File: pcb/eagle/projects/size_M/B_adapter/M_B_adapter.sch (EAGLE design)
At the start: 16 parts

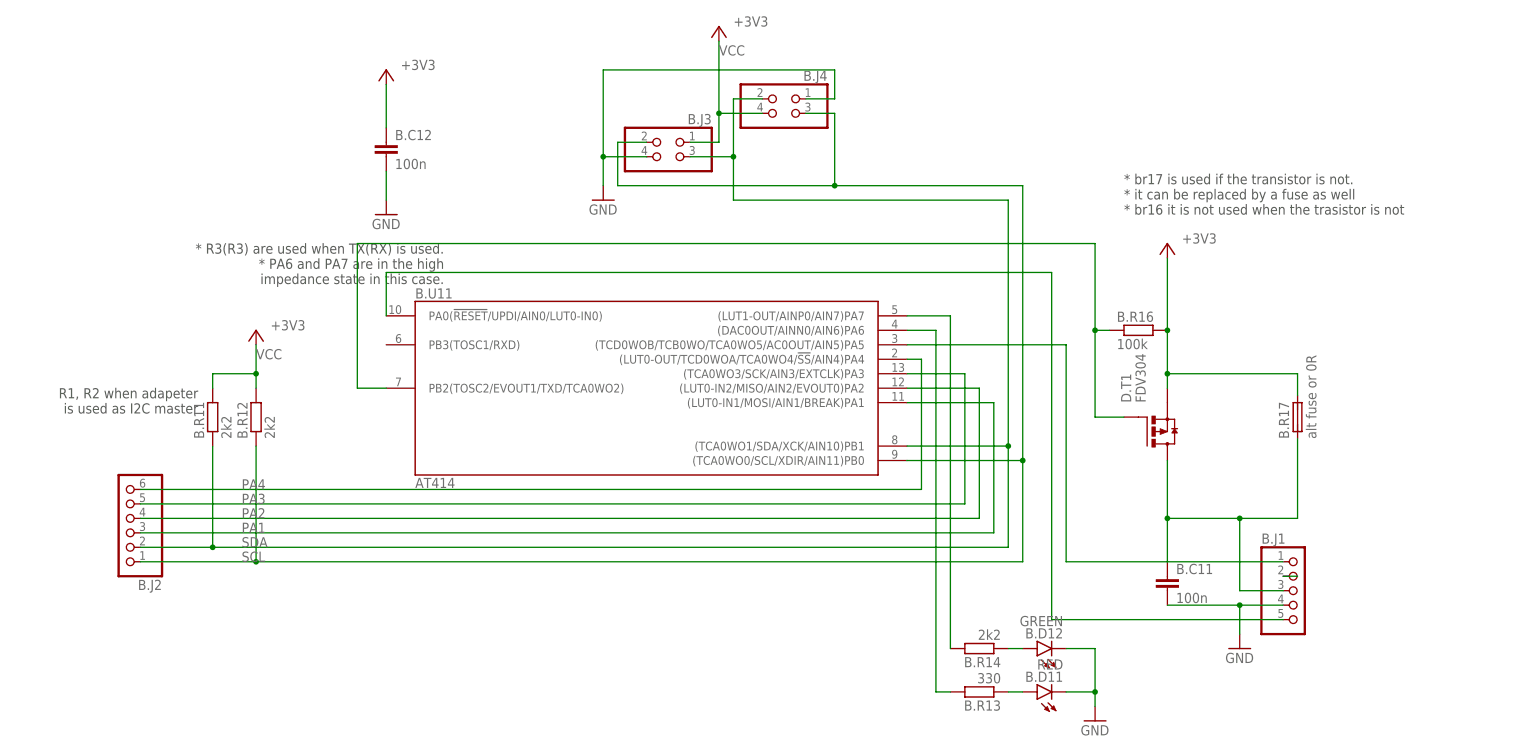
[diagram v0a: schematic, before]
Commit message: version 8 main changes * ideal diode separated 3v3 DC-DC to protect it from back current * smaller package of ina 219 * usage of tssop attiny v2 in adapter * and change of PA5 to PB2 with ^ and ~ (originally used for shield power switch - now PB3) * step motor shield * out signal for BT module
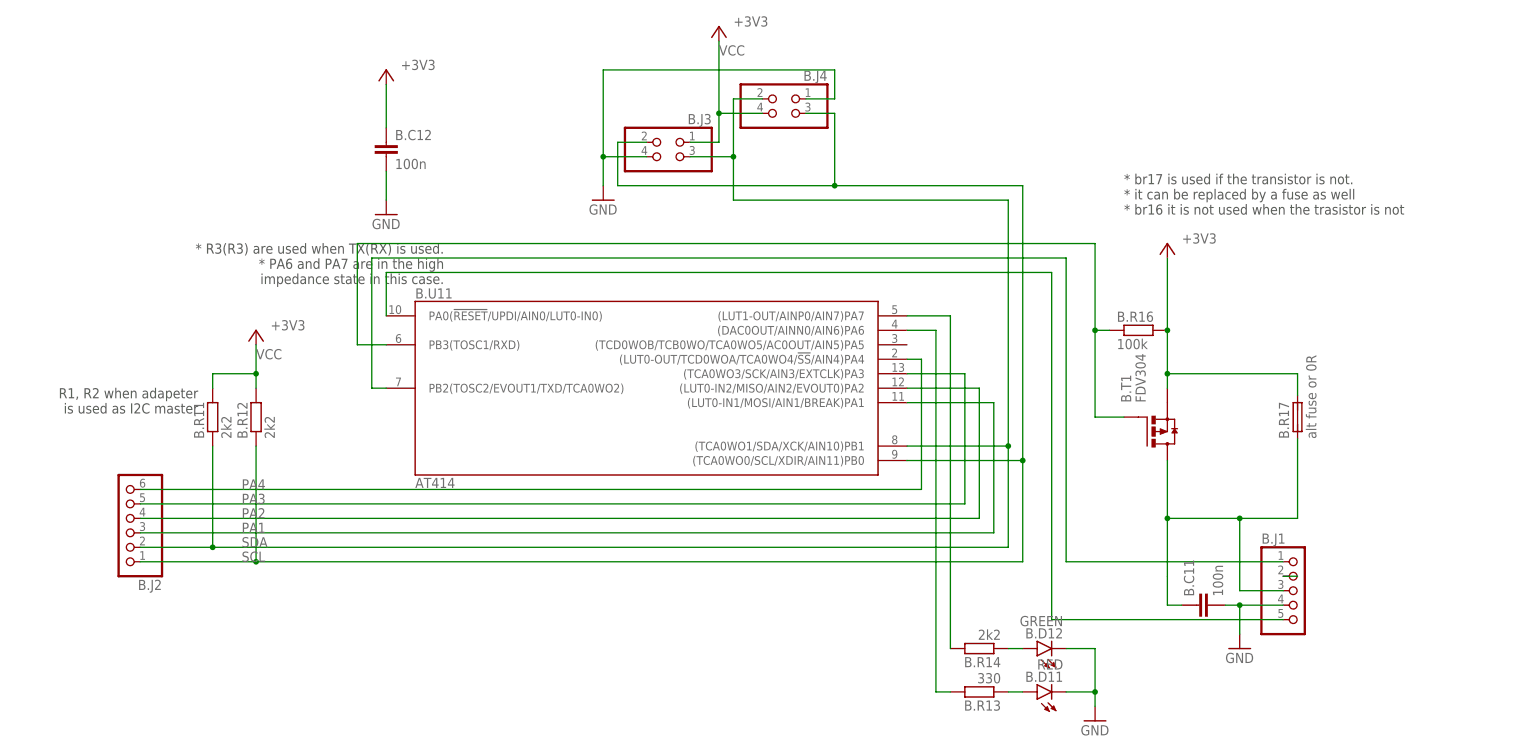
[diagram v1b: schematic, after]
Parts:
- renumbered D.T1 to B.T1
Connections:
- removed net PA5: B.J1.1, B.U11G$1.(TCD0WOB/TCB0WO/TCA0WO5/AC0OUT/AIN5)PA5
- new net PB3: B.R16.1, B.T1.G, B.U11G$1.PB3(TOSC1/RXD)
- net PB2: now also B.J1.1; no longer B.R16.1, B.T1.G
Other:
- moved on the sheet: B.C11
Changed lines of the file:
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@@
 <part name="B.R14" library="rcl" library_urn="urn:adsk.eagle:library:334" deviceset="R-EU_" device="R0603" package3d_urn="urn:adsk.eagle:package:23555/3" value="2k2"/>
 <part name="B.D12" library="led" deviceset="LED" device="CHIP-LED0603" package3d_urn="urn:adsk.eagle:package:15819/3" value="GREEN"/>
-<part name="D.T1" library="hugo" deviceset="P-MOSFET" device="" value="FDV304"/>
+<part name="B.T1" library="hugo" deviceset="P-MOSFET" device="" value="FDV304"/>
 </parts>
 <sheets>
@@
 <attribute name="VALUE" x="143.51" y="71.12" size="1.778" layer="96" rot="MR0"/>
 </instance>
-<instance part="B.C11" gate="G$1" x="203.2" y="-5.08" smashed="yes">
-<attribute name="NAME" x="204.724" y="-4.699" size="1.778" layer="95"/>
-<attribute name="VALUE" x="204.724" y="-9.779" size="1.778" layer="96"/>
+<instance part="B.C11" gate="G$1" x="208.28" y="-10.16" smashed="yes" rot="R90">
+<attribute name="NAME" x="207.899" y="-8.636" size="1.778" layer="95" rot="R90"/>
+<attribute name="VALUE" x="212.979" y="-8.636" size="1.778" layer="96" rot="R90"/>
 </instance>
 <instance part="B.J1" gate="A" x="226.06" y="-7.62" smashed="yes">
@@
 <attribute name="VALUE" x="184.912" y="-12.065" size="1.778" layer="96" rot="R180"/>
 </instance>
-<instance part="D.T1" gate="G$1" x="200.66" y="22.86" smashed="yes">
+<instance part="B.T1" gate="G$1" x="200.66" y="22.86" smashed="yes">
 <attribute name="NAME" x="196.85" y="25.4" size="1.778" layer="95" rot="R90"/>
 <attribute name="VALUE" x="199.39" y="25.4" size="1.778" layer="96" rot="R90"/>
@@
 <pinref part="B.C11" gate="G$1" pin="2"/>
 <pinref part="B.J1" gate="A" pin="4"/>
-<wire x1="203.2" y1="-10.16" x2="215.9" y2="-10.16" width="0.1524" layer="91"/>
+<wire x1="213.36" y1="-10.16" x2="215.9" y2="-10.16" width="0.1524" layer="91"/>
 <wire x1="215.9" y1="-10.16" x2="223.52" y2="-10.16" width="0.1524" layer="91"/>
 <pinref part="GND2" gate="1" pin="GND"/>
@@
 <pinref part="B.R17" gate="G$1" pin="2"/>
 <wire x1="226.06" y1="26.67" x2="226.06" y2="30.48" width="0.1524" layer="91"/>
-<pinref part="D.T1" gate="G$1" pin="S"/>
+<pinref part="B.T1" gate="G$1" pin="S"/>
 <pinref part="B.R16" gate="G$1" pin="2"/>
 <junction x="203.2" y="38.1"/>
@@
 <pinref part="B.C11" gate="G$1" pin="1"/>
 <wire x1="203.2" y1="15.24" x2="203.2" y2="5.08" width="0.1524" layer="91"/>
-<wire x1="203.2" y1="5.08" x2="203.2" y2="-2.54" width="0.1524" layer="91"/>
+<wire x1="203.2" y1="5.08" x2="203.2" y2="-5.08" width="0.1524" layer="91"/>
+<wire x1="203.2" y1="-5.08" x2="203.2" y2="-10.16" width="0.1524" layer="91"/>
+<wire x1="203.2" y1="-10.16" x2="205.74" y2="-10.16" width="0.1524" layer="91"/>
 <wire x1="203.2" y1="5.08" x2="215.9" y2="5.08" width="0.1524" layer="91"/>
 <wire x1="215.9" y1="5.08" x2="215.9" y2="-7.62" width="0.1524" layer="91"/>
@@
 <wire x1="215.9" y1="5.08" x2="226.06" y2="5.08" width="0.1524" layer="91"/>
 <wire x1="226.06" y1="5.08" x2="226.06" y2="19.05" width="0.1524" layer="91"/>
-<pinref part="D.T1" gate="G$1" pin="D"/>
+<pinref part="B.T1" gate="G$1" pin="D"/>
 </segment>
 </net>
@@
 </segment>
 </net>
-<net name="PB2" class="0">
+<net name="PB3" class="0">
 <segment>
 <wire x1="195.58" y1="22.86" x2="190.5" y2="22.86" width="0.1524" layer="91"/>
@@
 <wire x1="190.5" y1="38.1" x2="190.5" y2="53.34" width="0.1524" layer="91"/>
 <wire x1="190.5" y1="53.34" x2="60.96" y2="53.34" width="0.1524" layer="91"/>
-<wire x1="60.96" y1="53.34" x2="60.96" y2="27.94" width="0.1524" layer="91"/>
-<pinref part="B.U11" gate="G$1" pin="PB2(TOSC2/EVOUT1/TXD/TCA0WO2)"/>
-<wire x1="60.96" y1="27.94" x2="66.04" y2="27.94" width="0.1524" layer="91"/>
-<pinref part="D.T1" gate="G$1" pin="G"/>
+<wire x1="60.96" y1="53.34" x2="60.96" y2="35.56" width="0.1524" layer="91"/>
+<pinref part="B.T1" gate="G$1" pin="G"/>
 <pinref part="B.R16" gate="G$1" pin="1"/>
 <wire x1="193.04" y1="38.1" x2="190.5" y2="38.1" width="0.1524" layer="91"/>
 <junction x="190.5" y="38.1"/>
+<pinref part="B.U11" gate="G$1" pin="PB3(TOSC1/RXD)"/>
+<wire x1="66.04" y1="35.56" x2="60.96" y2="35.56" width="0.1524" layer="91"/>
 </segment>
 </net>
@@
 </segment>
 </net>
-<net name="PA5" class="0">
+<net name="PB2" class="0">
 <segment>
 <pinref part="B.J1" gate="A" pin="1"/>
-<wire x1="185.42" y1="35.56" x2="185.42" y2="-2.54" width="0.1524" layer="91"/>
+<wire x1="185.42" y1="50.8" x2="185.42" y2="-2.54" width="0.1524" layer="91"/>
 <wire x1="185.42" y1="-2.54" x2="223.52" y2="-2.54" width="0.1524" layer="91"/>
-<pinref part="B.U11" gate="G$1" pin="(TCD0WOB/TCB0WO/TCA0WO5/AC0OUT/AIN5)PA5"/>
-<wire x1="157.48" y1="35.56" x2="185.42" y2="35.56" width="0.1524" layer="91"/>
-</segment>
-</net>
+<pinref part="B.U11" gate="G$1" pin="PB2(TOSC2/EVOUT1/TXD/TCA0WO2)"/>
+<wire x1="63.5" y1="27.94" x2="66.04" y2="27.94" width="0.1524" layer="91"/>
+<wire x1="185.42" y1="50.8" x2="63.5" y2="50.8" width="0.1524" layer="91"/>
+<wire x1="63.5" y1="50.8" x2="63.5" y2="27.94" width="0.1524" layer="91"/>
+</segment>
+</net>

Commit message: PCB v9
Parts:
- removed B.J1: (no value), pinhead2:PINHD-1X5
- added B.J5: (no value), pinhead2:PINHD-1X6
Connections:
- new net PA6: B.J5.1, B.U11G$1.(DAC0OUT/AINN0/AIN6)PA6
- net GND: now also B.J5.4; no longer B.J1.4
- net N$4: now also B.J5.3; no longer B.J1.3
- net N$5: now also B.U11G$1.(TCD0WOB/TCB0WO/TCA0WO5/AC0OUT/AIN5)PA5; no longer B.U11G$1.(DAC0OUT/AINN0/AIN6)PA6
- net PB2: now also B.J5.6; no longer B.J1.1
- net UPDI: now also B.J5.5; no longer B.J1.5
- net VBAT: now also B.J5.2; no longer B.J1.2
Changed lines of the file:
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@@
 <part name="B.J4" library="pinhead2" deviceset="PINHD-2X2" device="" package3d_urn="urn:adsk.eagle:package:22455/2"/>
 <part name="B.C11" library="rcl" library_urn="urn:adsk.eagle:library:334" deviceset="C-EU" device="C0603" package3d_urn="urn:adsk.eagle:package:23616/2" value="100n"/>
-<part name="B.J1" library="pinhead2" deviceset="PINHD-1X5" device="" package3d_urn="urn:adsk.eagle:package:22469/2"/>
 <part name="GND2" library="supply1" library_urn="urn:adsk.eagle:library:371" deviceset="GND" device=""/>
 <part name="+3V2" library="supply1" library_urn="urn:adsk.eagle:library:371" deviceset="+3V3" device=""/>
@@
 <part name="B.D12" library="led" deviceset="LED" device="CHIP-LED0603" package3d_urn="urn:adsk.eagle:package:15819/3" value="GREEN"/>
 <part name="B.T1" library="hugo" deviceset="P-MOSFET" device="" value="FDV304"/>
+<part name="B.J5" library="pinhead2" deviceset="PINHD-1X6" device="" package3d_urn="urn:adsk.eagle:package:22472/2"/>
 </parts>
 <sheets>
@@
 <attribute name="VALUE" x="212.979" y="-8.636" size="1.778" layer="96" rot="R90"/>
 </instance>
-<instance part="B.J1" gate="A" x="226.06" y="-7.62" smashed="yes">
-<attribute name="NAME" x="219.71" y="0.635" size="1.778" layer="95"/>
-<attribute name="VALUE" x="219.71" y="-17.78" size="1.778" layer="96"/>
-</instance>
-<instance part="GND2" gate="1" x="215.9" y="-17.78" smashed="yes">
-<attribute name="VALUE" x="213.36" y="-20.32" size="1.778" layer="96"/>
+<instance part="GND2" gate="1" x="215.9" y="-22.86" smashed="yes">
+<attribute name="VALUE" x="213.36" y="-25.4" size="1.778" layer="96"/>
 </instance>
 <instance part="+3V2" gate="G$1" x="124.46" y="91.44" smashed="yes">
@@
 <attribute name="NAME" x="196.85" y="25.4" size="1.778" layer="95" rot="R90"/>
 <attribute name="VALUE" x="199.39" y="25.4" size="1.778" layer="96" rot="R90"/>
+</instance>
+<instance part="B.J5" gate="A" x="226.06" y="-10.16" smashed="yes">
+<attribute name="NAME" x="219.71" y="0.635" size="1.778" layer="95"/>
+<attribute name="VALUE" x="219.71" y="-20.32" size="1.778" layer="96"/>
 </instance>
 </instances>
@@
 <segment>
 <pinref part="B.C11" gate="G$1" pin="2"/>
-<pinref part="B.J1" gate="A" pin="4"/>
 <wire x1="213.36" y1="-10.16" x2="215.9" y2="-10.16" width="0.1524" layer="91"/>
 <wire x1="215.9" y1="-10.16" x2="223.52" y2="-10.16" width="0.1524" layer="91"/>
 <pinref part="GND2" gate="1" pin="GND"/>
-<wire x1="215.9" y1="-15.24" x2="215.9" y2="-10.16" width="0.1524" layer="91"/>
+<wire x1="215.9" y1="-20.32" x2="215.9" y2="-10.16" width="0.1524" layer="91"/>
 <junction x="215.9" y="-10.16"/>
+<pinref part="B.J5" gate="A" pin="4"/>
 </segment>
 <segment>
@@
 <net name="UPDI" class="0">
 <segment>
-<pinref part="B.J1" gate="A" pin="5"/>
 <pinref part="B.U11" gate="G$1" pin="PA0(!RESET!/UPDI/AIN0/LUT0-IN0)"/>
 <wire x1="182.88" y1="-12.7" x2="223.52" y2="-12.7" width="0.1524" layer="91"/>
@@
 <wire x1="66.04" y1="48.26" x2="182.88" y2="48.26" width="0.1524" layer="91"/>
 <wire x1="182.88" y1="48.26" x2="182.88" y2="-12.7" width="0.1524" layer="91"/>
+<pinref part="B.J5" gate="A" pin="5"/>
 </segment>
 </net>
@@
 <pinref part="B.C11" gate="G$1" pin="1"/>
 <wire x1="203.2" y1="15.24" x2="203.2" y2="5.08" width="0.1524" layer="91"/>
-<wire x1="203.2" y1="5.08" x2="203.2" y2="-5.08" width="0.1524" layer="91"/>
-<wire x1="203.2" y1="-5.08" x2="203.2" y2="-10.16" width="0.1524" layer="91"/>
+<wire x1="203.2" y1="5.08" x2="203.2" y2="-10.16" width="0.1524" layer="91"/>
 <wire x1="203.2" y1="-10.16" x2="205.74" y2="-10.16" width="0.1524" layer="91"/>
 <wire x1="203.2" y1="5.08" x2="215.9" y2="5.08" width="0.1524" layer="91"/>
 <wire x1="215.9" y1="5.08" x2="215.9" y2="-7.62" width="0.1524" layer="91"/>
 <junction x="203.2" y="5.08"/>
-<pinref part="B.J1" gate="A" pin="3"/>
 <wire x1="215.9" y1="-7.62" x2="223.52" y2="-7.62" width="0.1524" layer="91"/>
 <junction x="215.9" y="5.08"/>
@@
 <wire x1="226.06" y1="5.08" x2="226.06" y2="19.05" width="0.1524" layer="91"/>
 <pinref part="B.T1" gate="G$1" pin="D"/>
+<pinref part="B.J5" gate="A" pin="3"/>
 </segment>
 </net>
 <net name="VBAT" class="0">
 <segment>
-<pinref part="B.J1" gate="A" pin="2"/>
 <wire x1="223.52" y1="-5.08" x2="226.06" y2="-5.08" width="0.1524" layer="91"/>
+<pinref part="B.J5" gate="A" pin="2"/>
 </segment>
 </net>
@@
 <net name="PB2" class="0">
 <segment>
-<pinref part="B.J1" gate="A" pin="1"/>
-<wire x1="185.42" y1="50.8" x2="185.42" y2="-2.54" width="0.1524" layer="91"/>
-<wire x1="185.42" y1="-2.54" x2="223.52" y2="-2.54" width="0.1524" layer="91"/>
+<wire x1="185.42" y1="50.8" x2="185.42" y2="-10.16" width="0.1524" layer="91"/>
+<wire x1="185.42" y1="-10.16" x2="195.58" y2="-10.16" width="0.1524" layer="91"/>
 <pinref part="B.U11" gate="G$1" pin="PB2(TOSC2/EVOUT1/TXD/TCA0WO2)"/>
 <wire x1="63.5" y1="27.94" x2="66.04" y2="27.94" width="0.1524" layer="91"/>
 <wire x1="185.42" y1="50.8" x2="63.5" y2="50.8" width="0.1524" layer="91"/>
 <wire x1="63.5" y1="50.8" x2="63.5" y2="27.94" width="0.1524" layer="91"/>
+<wire x1="195.58" y1="-10.16" x2="195.58" y2="-15.24" width="0.1524" layer="91"/>
+<wire x1="195.58" y1="-15.24" x2="223.52" y2="-15.24" width="0.1524" layer="91"/>
+<pinref part="B.J5" gate="A" pin="6"/>
+<wire x1="223.52" y1="-15.24" x2="226.06" y2="-15.24" width="0.1524" layer="91"/>
+<junction x="223.52" y="-15.24"/>
 </segment>
 </net>
@@
 <pinref part="B.R13" gate="G$1" pin="2"/>
 <wire x1="165.1" y1="-25.4" x2="162.56" y2="-25.4" width="0.1524" layer="91"/>
-<wire x1="162.56" y1="-25.4" x2="162.56" y2="38.1" width="0.1524" layer="91"/>
+<wire x1="162.56" y1="-25.4" x2="162.56" y2="35.56" width="0.1524" layer="91"/>
+<pinref part="B.U11" gate="G$1" pin="(TCD0WOB/TCB0WO/TCA0WO5/AC0OUT/AIN5)PA5"/>
+<wire x1="157.48" y1="35.56" x2="162.56" y2="35.56" width="0.1524" layer="91"/>
+</segment>
+</net>
+<net name="PA6" class="0">
+<segment>
 <pinref part="B.U11" gate="G$1" pin="(DAC0OUT/AINN0/AIN6)PA6"/>
-<wire x1="162.56" y1="38.1" x2="157.48" y2="38.1" width="0.1524" layer="91"/>
-</segment>
-</net>
+<wire x1="157.48" y1="38.1" x2="187.96" y2="38.1" width="0.1524" layer="91"/>
+<wire x1="187.96" y1="38.1" x2="187.96" y2="-2.54" width="0.1524" layer="91"/>
+<wire x1="187.96" y1="-2.54" x2="223.52" y2="-2.54" width="0.1524" layer="91"/>
+<pinref part="B.J5" gate="A" pin="1"/>
+</segment>
+</net>
